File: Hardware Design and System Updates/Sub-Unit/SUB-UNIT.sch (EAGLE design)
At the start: 4 parts, among them U1 MSP430FR2000IPW16PW16_TEX

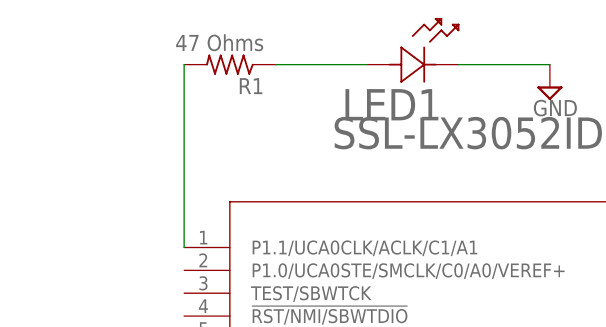
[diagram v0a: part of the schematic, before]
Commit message: Fixed R1 value
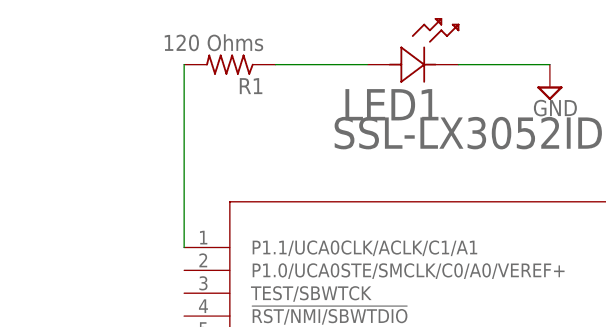
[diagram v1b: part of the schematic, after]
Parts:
- R1: value 47 Ohms -> 120 Ohms
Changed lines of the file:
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@@
 <part name="E1" library="HM-10 Bluetooth Module" deviceset="HM-10" device="-BOARD"/>
 <part name="LED1" library="Lumex SSL-LX3052ID RED LED" deviceset="SSL-LX3052ID" device=""/>
-<part name="R1" library="adafruit" deviceset="R-US_" device="0204/5" value="47 Ohms"/>
+<part name="R1" library="adafruit" deviceset="R-US_" device="0204/5" value="120 Ohms"/>
 <part name="U1" library="MSP430FR2000 Sub-Unit" deviceset="MSP430FR2000IPW16" device="PW16_TEX"/>
 <part name="SUPPLY2" library="supply2" library_urn="urn:adsk.eagle:library:372" deviceset="GND" device=""/>
